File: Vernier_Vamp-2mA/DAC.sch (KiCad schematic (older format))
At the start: 56 parts, among them U10 OPA2277, U11 OPA2277, U7 LTC6655-2.5, U8 DAC8814, U9 OPA2277

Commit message: 1.0B fixes for 2mA (schematic)
Added 1.0B fixes to the 2mA version related to schematic cleanup, and addition of hysteresis and alternative way to power nano.
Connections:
- net labels added: +7.5V, -7.5V
- net labels removed: +8V, -8V
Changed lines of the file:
@@
 $Descr A4 11693 8268
 encoding utf-8
-Sheet 3 5
-Title "\"Vernier Vamp\" Coil Driver - 200mA"
-Date "2020-02-04"
-Rev "1.0A"
+Sheet 4 7
+Title "\"Vernier Vamp\" Coil Driver - 2mA"
+Date "2020-05-05"
+Rev "1.0B"
 Comp "Strathclyde University"
 Comment1 "Designed by: Marcin Mrozowski"
@@
 Text Notes 5500 5250 0    50   ~ 0
 Low power switching\nno need to connect it \nto digital ground\n
-$Comp
-L power:-8V #PWR?
-U 1 1 61AFD0B1
-P 950 7000
-AR Path="/5E1DD6A9/61AFD0B1" Ref="#PWR?"  Part="1"
-AR Path="/5E1DD476/61AFD0B1" Ref="#PWR0132"  Part="1"
-F 0 "#PWR0132" H 950 7100 50  0001 C CNN
-F 1 "-8V" H 965 7173 50  0000 C CNN
-F 2 "" H 950 7000 50  0001 C CNN
-F 3 "" H 950 7000 50  0001 C CNN
-	1    950  7000
-	-1   0    0    1
-$EndComp
-$Comp
-L power:-8V #PWR?
-U 1 1 61B2FD4A
-P 7600 2250
-AR Path="/5E1DD6A9/61B2FD4A" Ref="#PWR?"  Part="1"
-AR Path="/5E1DD476/61B2FD4A" Ref="#PWR0139"  Part="1"
-F 0 "#PWR0139" H 7600 2350 50  0001 C CNN
-F 1 "-8V" H 7615 2423 50  0000 C CNN
-F 2 "" H 7600 2250 50  0001 C CNN
-F 3 "" H 7600 2250 50  0001 C CNN
-	1    7600 2250
-	-1   0    0    1
-$EndComp
-$Comp
-L power:-8V #PWR?
-U 1 1 61B3C8E0
-P 7600 3650
-AR Path="/5E1DD6A9/61B3C8E0" Ref="#PWR?"  Part="1"
-AR Path="/5E1DD476/61B3C8E0" Ref="#PWR0141"  Part="1"
-F 0 "#PWR0141" H 7600 3750 50  0001 C CNN
-F 1 "-8V" H 7615 3823 50  0000 C CNN
-F 2 "" H 7600 3650 50  0001 C CNN
-F 3 "" H 7600 3650 50  0001 C CNN
-	1    7600 3650
-	-1   0    0    1
-$EndComp
-$Comp
-L power:-8V #PWR?
-U 1 1 61B495DC
-P 7600 5050
-AR Path="/5E1DD6A9/61B495DC" Ref="#PWR?"  Part="1"
-AR Path="/5E1DD476/61B495DC" Ref="#PWR0143"  Part="1"
-F 0 "#PWR0143" H 7600 5150 50  0001 C CNN
-F 1 "-8V" H 7615 5223 50  0000 C CNN
-F 2 "" H 7600 5050 50  0001 C CNN
-F 3 "" H 7600 5050 50  0001 C CNN
-	1    7600 5050
-	-1   0    0    1
-$EndComp
-$Comp
-L power:+8V #PWR?
-U 1 1 61C34E64
-P 7600 4450
-AR Path="/5E1DD6A9/61C34E64" Ref="#PWR?"  Part="1"
-AR Path="/5E1DD476/61C34E64" Ref="#PWR0145"  Part="1"
-F 0 "#PWR0145" H 7600 4300 50  0001 C CNN
-F 1 "+8V" H 7615 4623 50  0000 C CNN
-F 2 "" H 7600 4450 50  0001 C CNN
-F 3 "" H 7600 4450 50  0001 C CNN
-	1    7600 4450
-	1    0    0    -1
-$EndComp
-$Comp
-L power:+8V #PWR?
-U 1 1 61C41B21
-P 7600 3050
-AR Path="/5E1DD6A9/61C41B21" Ref="#PWR?"  Part="1"
-AR Path="/5E1DD476/61C41B21" Ref="#PWR0149"  Part="1"
-F 0 "#PWR0149" H 7600 2900 50  0001 C CNN
-F 1 "+8V" H 7615 3223 50  0000 C CNN
-F 2 "" H 7600 3050 50  0001 C CNN
-F 3 "" H 7600 3050 50  0001 C CNN
-	1    7600 3050
-	1    0    0    -1
-$EndComp
-$Comp
-L power:+8V #PWR?
-U 1 1 61C4E787
-P 7600 1650
-AR Path="/5E1DD6A9/61C4E787" Ref="#PWR?"  Part="1"
-AR Path="/5E1DD476/61C4E787" Ref="#PWR0150"  Part="1"
-F 0 "#PWR0150" H 7600 1500 50  0001 C CNN
-F 1 "+8V" H 7615 1823 50  0000 C CNN
-F 2 "" H 7600 1650 50  0001 C CNN
-F 3 "" H 7600 1650 50  0001 C CNN
-	1    7600 1650
-	1    0    0    -1
-$EndComp
-$Comp
-L power:+8V #PWR?
-U 1 1 61C67E10
-P 750 1100
-AR Path="/5E1DD6A9/61C67E10" Ref="#PWR?"  Part="1"
-AR Path="/5E1DD476/61C67E10" Ref="#PWR0151"  Part="1"
-F 0 "#PWR0151" H 750 950 50  0001 C CNN
-F 1 "+8V" H 765 1273 50  0000 C CNN
-F 2 "" H 750 1100 50  0001 C CNN
-F 3 "" H 750 1100 50  0001 C CNN
-	1    750  1100
-	1    0    0    -1
-$EndComp
-$Comp
-L power:+8V #PWR?
-U 1 1 61C813CA
-P 950 5750
-AR Path="/5E1DD6A9/61C813CA" Ref="#PWR?"  Part="1"
-AR Path="/5E1DD476/61C813CA" Ref="#PWR0152"  Part="1"
-F 0 "#PWR0152" H 950 5600 50  0001 C CNN
-F 1 "+8V" H 965 5923 50  0000 C CNN
-F 2 "" H 950 5750 50  0001 C CNN
-F 3 "" H 950 5750 50  0001 C CNN
-	1    950  5750
-	1    0    0    -1
-$EndComp
 Wire Notes Line
 	8150 2750 6600 2750
@@
 	5150 4550 5250 4550
 Connection ~ 5250 4550
+$Comp
+L custom_power_rails:+7.5V #PWR?
+U 1 1 5EF43E88
+P 750 1100
+AR Path="/5E1DD6A9/5EC279B2/5EF43E88" Ref="#PWR?"  Part="1"
+AR Path="/5E1DD476/5EF43E88" Ref="#PWR0151"  Part="1"
+F 0 "#PWR0151" H 750 1050 50  0001 C CNN
+F 1 "+7.5V" H 735 1273 50  0000 C CNN
+F 2 "" H 750 1100 50  0001 C CNN
+F 3 "" H 750 1100 50  0001 C CNN
+	1    750  1100
+	1    0    0    -1
+$EndComp
+$Comp
+L custom_power_rails:+7.5V #PWR?
+U 1 1 5EF6397B
+P 7600 4450
+AR Path="/5E1DD6A9/5EC279B2/5EF6397B" Ref="#PWR?"  Part="1"
+AR Path="/5E1DD476/5EF6397B" Ref="#PWR0152"  Part="1"
+F 0 "#PWR0152" H 7600 4400 50  0001 C CNN
+F 1 "+7.5V" H 7585 4623 50  0000 C CNN
+F 2 "" H 7600 4450 50  0001 C CNN
+F 3 "" H 7600 4450 50  0001 C CNN
+	1    7600 4450
+	1    0    0    -1
+$EndComp
+$Comp
+L custom_power_rails:+7.5V #PWR?
+U 1 1 5EF73240
+P 7600 3050
+AR Path="/5E1DD6A9/5EC279B2/5EF73240" Ref="#PWR?"  Part="1"
+AR Path="/5E1DD476/5EF73240" Ref="#PWR0155"  Part="1"
+F 0 "#PWR0155" H 7600 3000 50  0001 C CNN
+F 1 "+7.5V" H 7585 3223 50  0000 C CNN
+F 2 "" H 7600 3050 50  0001 C CNN
+F 3 "" H 7600 3050 50  0001 C CNN
+	1    7600 3050
+	1    0    0    -1
+$EndComp
+$Comp
+L custom_power_rails:+7.5V #PWR?
+U 1 1 5EF92C6D
+P 7600 1650
+AR Path="/5E1DD6A9/5EC279B2/5EF92C6D" Ref="#PWR?"  Part="1"
+AR Path="/5E1DD476/5EF92C6D" Ref="#PWR0158"  Part="1"
+F 0 "#PWR0158" H 7600 1600 50  0001 C CNN
+F 1 "+7.5V" H 7585 1823 50  0000 C CNN
+F 2 "" H 7600 1650 50  0001 C CNN
+F 3 "" H 7600 1650 50  0001 C CNN
+	1    7600 1650
+	1    0    0    -1
+$EndComp
+$Comp
+L custom_power_rails:+7.5V #PWR?
+U 1 1 5EFB1CFC
+P 950 5750
+AR Path="/5E1DD6A9/5EC279B2/5EFB1CFC" Ref="#PWR?"  Part="1"
+AR Path="/5E1DD476/5EFB1CFC" Ref="#PWR0162"  Part="1"
+F 0 "#PWR0162" H 950 5700 50  0001 C CNN
+F 1 "+7.5V" H 935 5923 50  0000 C CNN
+F 2 "" H 950 5750 50  0001 C CNN
+F 3 "" H 950 5750 50  0001 C CNN
+	1    950  5750
+	1    0    0    -1
+$EndComp
+$Comp
+L custom_power_rails:-7.5V #PWR?
+U 1 1 5EFF5F28
+P 950 7000
+AR Path="/5E1DD6A9/5EC279B2/5EFF5F28" Ref="#PWR?"  Part="1"
+AR Path="/5E1DD6A9/5EFF5F28" Ref="#PWR?"  Part="1"
+AR Path="/5E1DD476/5EFF5F28" Ref="#PWR0171"  Part="1"
+F 0 "#PWR0171" H 950 6950 50  0001 C CNN
+F 1 "-7.5V" H 935 7173 50  0000 C CNN
+F 2 "" H 950 7000 50  0001 C CNN
+F 3 "" H 950 7000 50  0001 C CNN
+	1    950  7000
+	-1   0    0    1
+$EndComp
+$Comp
+L custom_power_rails:-7.5V #PWR?
+U 1 1 5F015856
+P 7600 5050
+AR Path="/5E1DD6A9/5EC279B2/5F015856" Ref="#PWR?"  Part="1"
+AR Path="/5E1DD6A9/5F015856" Ref="#PWR?"  Part="1"
+AR Path="/5E1DD476/5F015856" Ref="#PWR0173"  Part="1"
+F 0 "#PWR0173" H 7600 5000 50  0001 C CNN
+F 1 "-7.5V" H 7585 5223 50  0000 C CNN
+F 2 "" H 7600 5050 50  0001 C CNN
+F 3 "" H 7600 5050 50  0001 C CNN
+	1    7600 5050
+	-1   0    0    1
+$EndComp
+$Comp
+L custom_power_rails:-7.5V #PWR?
+U 1 1 5F0250E3
+P 7600 3650
+AR Path="/5E1DD6A9/5EC279B2/5F0250E3" Ref="#PWR?"  Part="1"
+AR Path="/5E1DD6A9/5F0250E3" Ref="#PWR?"  Part="1"
+AR Path="/5E1DD476/5F0250E3" Ref="#PWR0176"  Part="1"
+F 0 "#PWR0176" H 7600 3600 50  0001 C CNN
+F 1 "-7.5V" H 7585 3823 50  0000 C CNN
+F 2 "" H 7600 3650 50  0001 C CNN
+F 3 "" H 7600 3650 50  0001 C CNN
+	1    7600 3650
+	-1   0    0    1
+$EndComp
+$Comp
+L custom_power_rails:-7.5V #PWR?
+U 1 1 5F0349B1
+P 7600 2250
+AR Path="/5E1DD6A9/5EC279B2/5F0349B1" Ref="#PWR?"  Part="1"
+AR Path="/5E1DD6A9/5F0349B1" Ref="#PWR?"  Part="1"
+AR Path="/5E1DD476/5F0349B1" Ref="#PWR0177"  Part="1"
+F 0 "#PWR0177" H 7600 2200 50  0001 C CNN
+F 1 "-7.5V" H 7585 2423 50  0000 C CNN
+F 2 "" H 7600 2250 50  0001 C CNN
+F 3 "" H 7600 2250 50  0001 C CNN
+	1    7600 2250
+	-1   0    0    1
+$EndComp
 $EndSCHEMATC

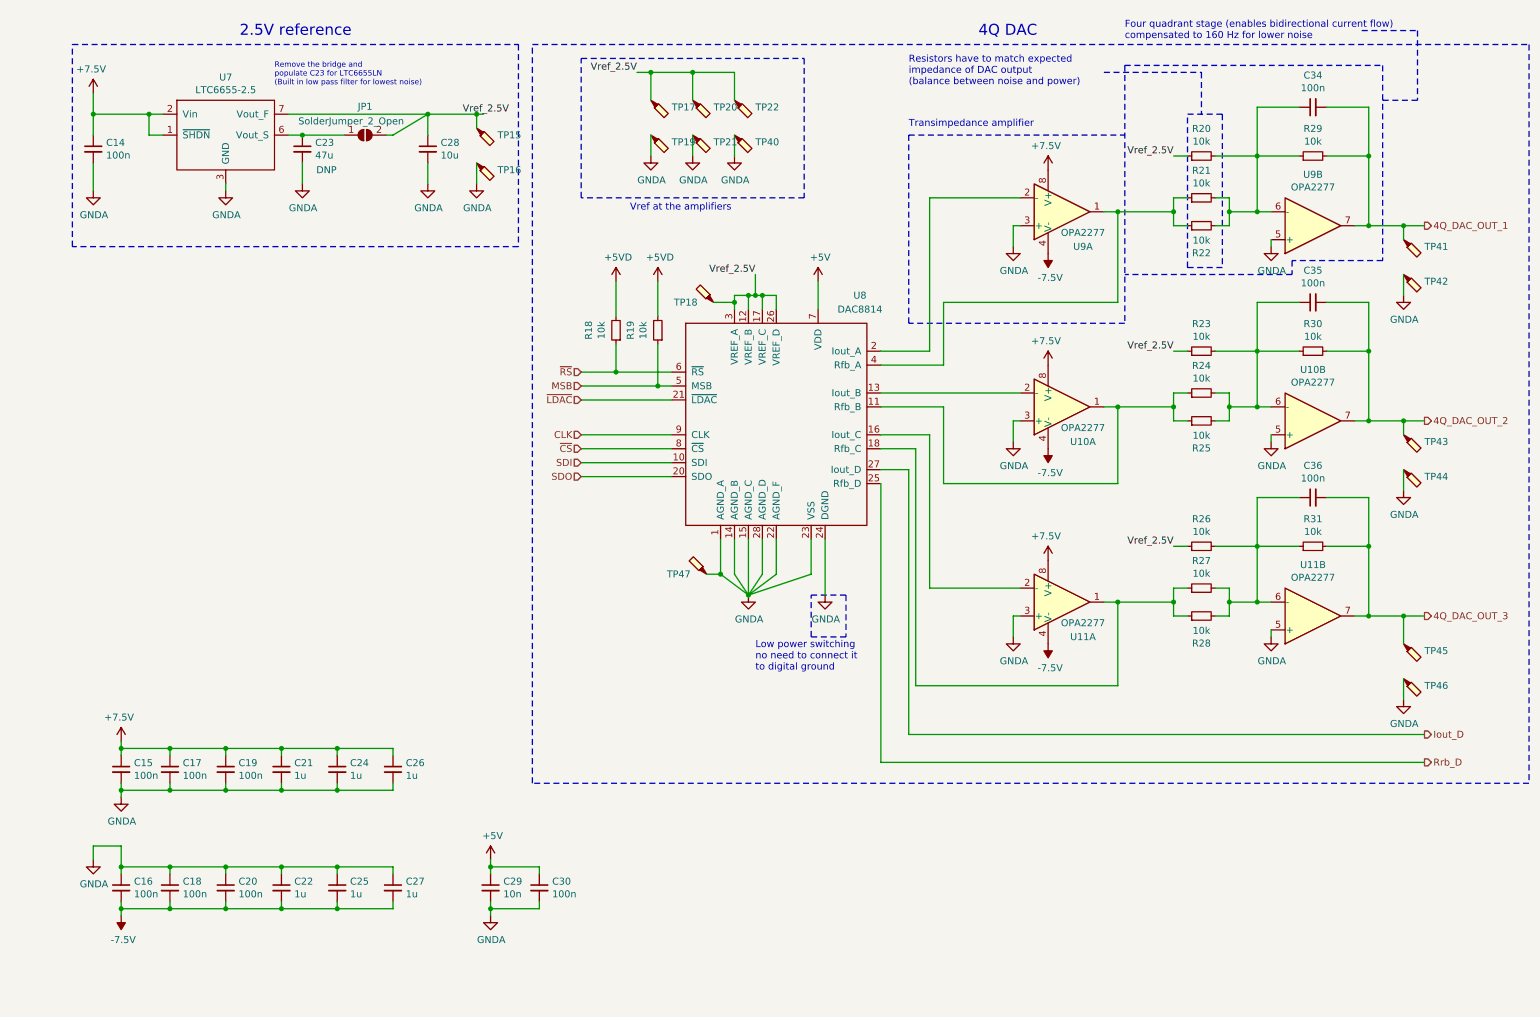
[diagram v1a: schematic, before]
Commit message: Applied 1.0B changes to 2mA version
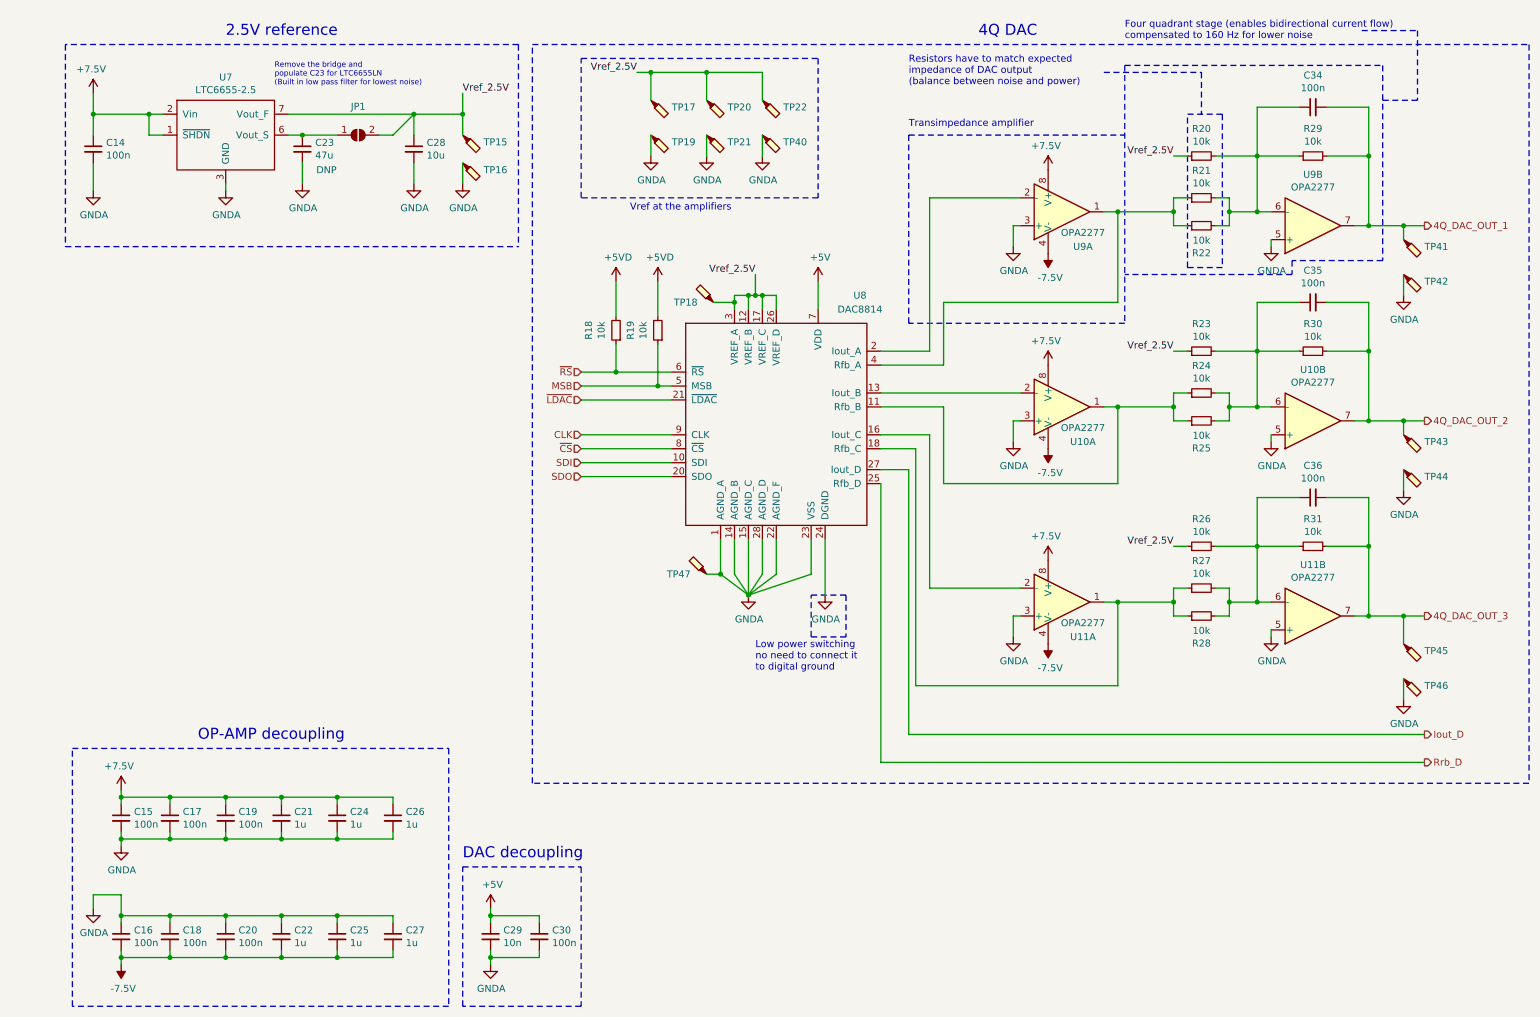
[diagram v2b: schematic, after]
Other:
- note added: "DAC decoupling\n"
- note added: "OP-AMP decoupling\n"
- moved on the sheet: C15, C16, C17, C18, C19, C20, C21, C22, C24, C25, C26, C27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
